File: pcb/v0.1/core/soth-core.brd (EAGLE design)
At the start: 54 x 22 mm, 31 parts, among them IC1 ATXMEGA32E5-AU, M1 SMALL_SERVO, M2 SMALL_SERVO, M3 SMALL_SERVO, M4 SMALL_SERVO, M5 SMALL_SERVO, U1 LDO-TPS78233

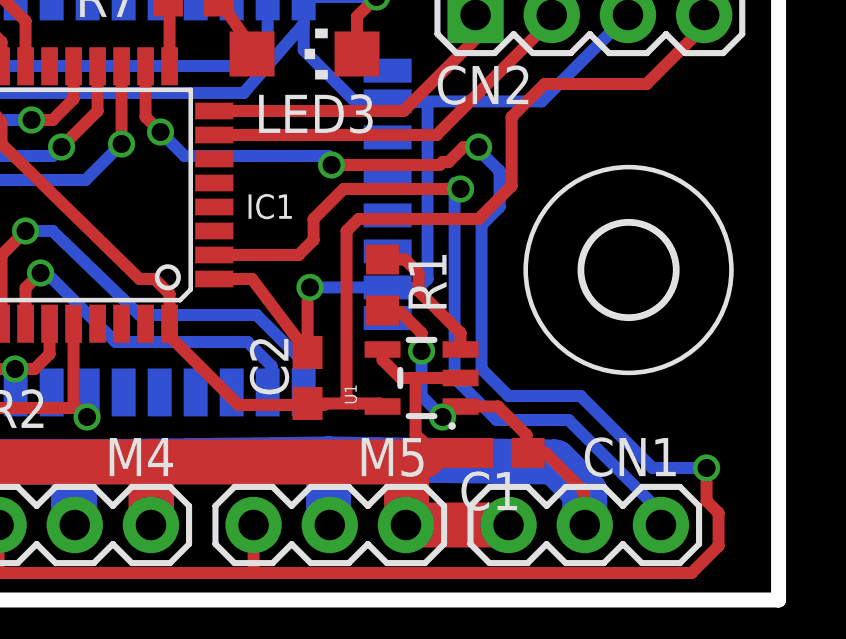
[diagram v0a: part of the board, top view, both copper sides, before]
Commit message: Bugfix pcb design. Replace LDO parts.
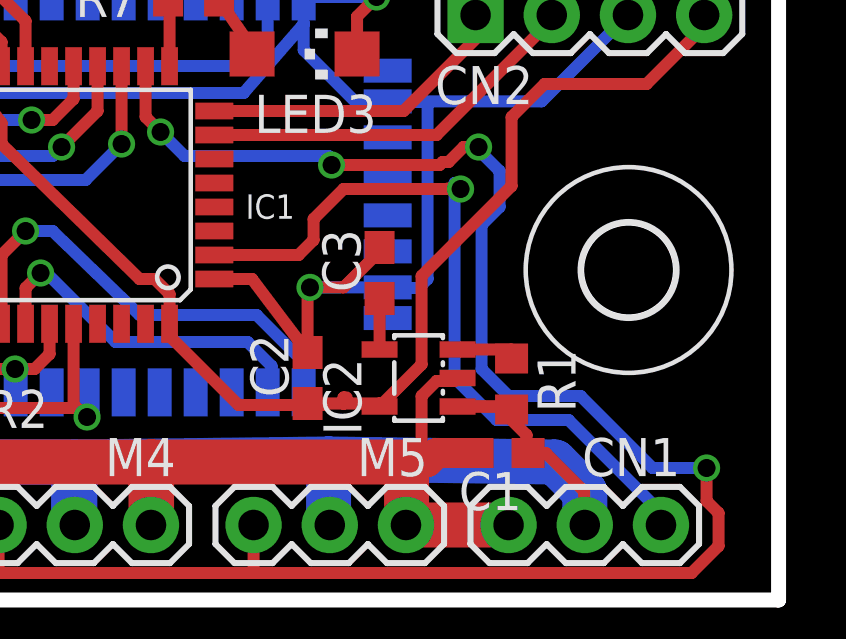
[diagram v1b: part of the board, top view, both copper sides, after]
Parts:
- removed U1: LDO-TPS78233, SparkFun-PowerIC:SOT23-5
- added C3: 0u01, rcl:C1608
- added IC2: TPS77001, texas:SOT23-DBV
- moved R1 5.42 mm to (45.1, 7.20)
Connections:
- new net N$25: C3.1, IC2.4
- net +3V3: now also IC2.5; no longer U1.5
- net +5V: now also IC2.1; no longer U1.1
- net GND: now also IC2.2; no longer U1.2, U1.4
- net GNDA: now also C3.2
- net N$2: now also IC2.3; no longer U1.3
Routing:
- net +5V: track 90.0 -> 86.2 mm, vias 4 -> 2
- net GND: track 83.9 -> 80.3 mm
- net GNDA: track 113.2 -> 116.2 mm
- net +3V3: track 86.2 -> 83.6 mm
- net N$2: track 4.52 -> 2.10 mm
- net N$25: track 0.00 -> 1.70 mm
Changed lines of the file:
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@@
 <attribute name="VALUE" x="43.73" y="-0.675" size="1.27" layer="27"/>
 </element>
-<element name="U1" library="SparkFun-PowerIC" package="SOT23-5" value="LDO-TPS78233" x="42.1" y="7.4" rot="R90"/>
 <element name="C1" library="rcl" package="C1608" value="0u1" x="44.8" y="4.9" rot="R180"/>
 <element name="C2" library="rcl" package="C1608" value="1u" x="38.3" y="7.4" rot="R90"/>
-<element name="R1" library="rcl" package="R0603" value="10k" x="40.8" y="10.5" smashed="yes" rot="R90">
-<attribute name="NAME" x="42.9336" y="9.5602" size="1.27" layer="25" rot="R90"/>
-<attribute name="VALUE" x="42.705" y="9.865" size="1.27" layer="27" rot="R90"/>
+<element name="R1" library="rcl" package="R0603" value="10k" x="45.1" y="7.2" smashed="yes" rot="R90">
+<attribute name="NAME" x="47.2336" y="6.2602" size="1.27" layer="25" rot="R90"/>
+<attribute name="VALUE" x="47.005" y="6.565" size="1.27" layer="27" rot="R90"/>
 </element>
 <element name="CN2" library="SparkFun-Connectors" package="1X04" value="" x="43.9" y="19.5" smashed="yes">
@@
 </element>
 <element name="U$2" library="Soth" package="SILK_LOGO" value="SOTH_LOGO" x="15.0622" y="17.9324"/>
+<element name="IC2" library="texas" package="SOT23-DBV" value="TPS77001" x="42" y="7.4" rot="R90">
+<attribute name="OC_NEWARK" value="77C1171" x="42" y="7.4" size="1.778" layer="27" rot="R90" display="off"/>
+<attribute name="MPN" value="TPS77001DBVT" x="42" y="7.4" size="1.778" layer="27" rot="R90" display="off"/>
+<attribute name="MF" value="TEXAS INSTRUMENTS" x="42" y="7.4" size="1.778" layer="27" rot="R90" display="off"/>
+<attribute name="OC_FARNELL" value="8461554" x="42" y="7.4" size="1.778" layer="27" rot="R90" display="off"/>
+</element>
+<element name="C3" library="rcl" package="C1608" value="0u01" x="40.7" y="10.9" rot="R90"/>
 </elements>
 <signals>
@@
 <wire x1="45" y1="2.5" x2="41.58" y2="2.5" width="1.5" layer="1"/>
 <contactref element="C1" pad="2"/>
-<contactref element="U1" pad="4"/>
-<contactref element="U1" pad="2"/>
 <wire x1="41.6" y1="4.6" x2="42.3" y2="4.6" width="1" layer="1"/>
 <wire x1="42.3" y1="4.6" x2="42.6" y2="4.9" width="1" layer="1"/>
 <wire x1="42.6" y1="4.9" x2="43.95" y2="4.9" width="1" layer="1"/>
-<wire x1="40.7999" y1="8.35" x2="40.7999" y2="8.0001" width="0.4" layer="1"/>
-<wire x1="40.7999" y1="8.0001" x2="41.4" y2="7.4" width="0.4" layer="1"/>
-<wire x1="41.4" y1="7.4" x2="43.4001" y2="7.4" width="0.4" layer="1"/>
-<wire x1="43.4001" y1="7.4" x2="42.1" y2="7.4" width="0.4" layer="1"/>
-<wire x1="42.1" y1="7.4" x2="41.9" y2="7.3" width="0.4" layer="1"/>
-<wire x1="41.9" y1="7.3" x2="41.9" y2="5.5" width="0.4" layer="1"/>
-<wire x1="41.9" y1="5.5" x2="42.6" y2="4.9" width="0.4" layer="1"/>
 <contactref element="T3" pad="2"/>
 <contactref element="T2" pad="2"/>
@@
 <wire x1="4.7" y1="4.892" x2="7.308" y2="4.892" width="0.4" layer="1"/>
 <wire x1="7.308" y1="4.892" x2="7.6" y2="4.6" width="0.4" layer="1"/>
+<contactref element="IC2" pad="2"/>
+<wire x1="42.6" y1="4.9" x2="42.1" y2="4.9" width="0.4" layer="1"/>
+<wire x1="42.1" y1="4.9" x2="42.1" y2="6.8" width="0.4" layer="1"/>
+<wire x1="42.1" y1="6.8" x2="42.6" y2="7.3" width="0.4" layer="1"/>
+<wire x1="42.6" y1="7.3" x2="43.2" y2="7.3" width="0.4" layer="1"/>
+<wire x1="43.2" y1="7.3" x2="43.3" y2="7.4" width="0.4" layer="1"/>
 </signal>
 <signal name="GNDA" class="4">
@@
 <vertex x="0" y="0"/>
 </polygon>
+<contactref element="C3" pad="2"/>
+<wire x1="40.7" y1="11.75" x2="40.7" y2="11.62" width="0.4" layer="1"/>
+<wire x1="40.7" y1="11.62" x2="39.5" y2="10.42" width="0.4" layer="1"/>
+<wire x1="39.5" y1="10.42" x2="38.38" y2="10.42" width="0.4" layer="1"/>
 </signal>
 <signal name="+3V3" class="3">
 <contactref element="IC1" pad="17"/>
 <contactref element="IC1" pad="32"/>
-<contactref element="U1" pad="5"/>
 <contactref element="C2" pad="1"/>
-<wire x1="38.3" y1="6.55" x2="39.9" y2="6.55" width="0.4" layer="1"/>
-<wire x1="39.9" y1="6.55" x2="40.6999" y2="6.55" width="0.4" layer="1"/>
-<wire x1="40.6999" y1="6.55" x2="40.7999" y2="6.45" width="0.4" layer="1"/>
 <contactref element="U$1" pad="11"/>
 <contactref element="CN2" pad="4"/>
@@
 <wire x1="51.52" y1="19.12" x2="49.6" y2="17.2" width="0.4" layer="1"/>
 <wire x1="49.6" y1="17.2" x2="46.2" y2="17.2" width="0.4" layer="1"/>
-<wire x1="39.6" y1="6.75" x2="39.9" y2="6.55" width="0.4" layer="1"/>
 <contactref element="R6" pad="2"/>
 <contactref element="R5" pad="2"/>
-<wire x1="39.6" y1="6.75" x2="39.6" y2="12.3" width="0.4" layer="1"/>
-<wire x1="39.6" y1="12.3" x2="40" y2="12.7" width="0.4" layer="1"/>
-<wire x1="40" y1="12.7" x2="44" y2="12.7" width="0.4" layer="1"/>
-<wire x1="44" y1="12.7" x2="45.1" y2="13.8" width="0.4" layer="1"/>
 <wire x1="45.1" y1="13.8" x2="45.1" y2="16.1" width="0.4" layer="1"/>
 <wire x1="45.1" y1="16.1" x2="46.2" y2="17.2" width="0.4" layer="1"/>
@@
 <wire x1="23.9" y1="18.3" x2="26.3" y2="18.3" width="0.4" layer="1"/>
 <wire x1="26.3" y1="18.3" x2="26.6" y2="18" width="0.4" layer="1"/>
+<contactref element="IC2" pad="5"/>
+<wire x1="38.3" y1="6.55" x2="39.5" y2="6.55" width="0.4064" layer="1"/>
+<wire x1="39.5" y1="6.55" x2="40.7" y2="6.55" width="0.4064" layer="1"/>
+<wire x1="40.7" y1="6.55" x2="40.7" y2="6.45" width="0.4064" layer="1"/>
+<wire x1="39.6" y1="6.75" x2="39.5" y2="6.75" width="0.4064" layer="1"/>
+<wire x1="39.5" y1="6.75" x2="39.5" y2="6.55" width="0.4064" layer="1"/>
+<wire x1="45.1" y1="13.8" x2="42.1" y2="10.8" width="0.4" layer="1"/>
+<wire x1="42.1" y1="10.8" x2="42.1" y2="7.85" width="0.4" layer="1"/>
+<wire x1="42.1" y1="7.85" x2="40.7" y2="6.45" width="0.4" layer="1"/>
 </signal>
 <signal name="+5V" class="1">
@@
 <wire x1="46.54" y1="4.6" x2="47.54" y2="3.6" width="1.5" layer="16"/>
 <wire x1="47.54" y1="3.6" x2="47.54" y2="2.5" width="1.5" layer="16"/>
-<contactref element="U1" pad="1"/>
 <contactref element="C1" pad="1"/>
-<contactref element="R1" pad="1"/>
 <wire x1="45.65" y1="4.9" x2="46.24" y2="4.9" width="0.4" layer="1"/>
 <wire x1="46.24" y1="4.9" x2="47.52" y2="3.62" width="0.4" layer="1"/>
 <wire x1="47.52" y1="3.62" x2="47.52" y2="2.52" width="0.4" layer="1"/>
 <wire x1="47.52" y1="2.52" x2="47.54" y2="2.5" width="0.4" layer="1"/>
-<wire x1="40.8" y1="9.65" x2="41.15" y2="9.65" width="0.4" layer="1"/>
-<wire x1="43.3501" y1="6.5" x2="43.4001" y2="6.45" width="0.4" layer="1"/>
-<wire x1="43.4001" y1="6.45" x2="44.65" y2="6.45" width="0.4" layer="1"/>
 <wire x1="44.65" y1="6.45" x2="45.6" y2="5.5" width="0.4" layer="1"/>
 <wire x1="45.6" y1="5.5" x2="45.6" y2="4.95" width="0.4" layer="1"/>
 <wire x1="45.6" y1="4.95" x2="45.65" y2="4.9" width="0.4" layer="1"/>
-<wire x1="43.3501" y1="6.5" x2="43.2" y2="6.5" width="0.4" layer="1"/>
-<wire x1="43.2" y1="6.5" x2="42.8" y2="6.1" width="0.4" layer="1"/>
-<via x="42.8" y="6.1" extent="1-16" drill="0.6"/>
-<wire x1="42.8" y1="6.1" x2="42.1" y2="6.8" width="0.4" layer="16"/>
-<wire x1="42.1" y1="6.8" x2="42.1" y2="8.3" width="0.4" layer="16"/>
-<via x="42.1" y="8.3" extent="1-16" drill="0.6"/>
-<wire x1="42.1" y1="8.3" x2="42.1" y2="8.9" width="0.4" layer="1"/>
-<wire x1="42.1" y1="8.9" x2="41.4" y2="9.6" width="0.4" layer="1"/>
-<wire x1="41.4" y1="9.6" x2="40.85" y2="9.6" width="0.4" layer="1"/>
-<wire x1="40.85" y1="9.6" x2="40.8" y2="9.65" width="0.4" layer="1"/>
 <contactref element="CN4" pad="1"/>
 <wire x1="5.04" y1="4.6" x2="4.14" y2="5.16" width="1" layer="16"/>
@@
 <wire x1="4.14" y1="5.16" x2="4.14" y2="8.74" width="1" layer="16"/>
 <wire x1="4.14" y1="8.74" x2="4.5" y2="9.1" width="1" layer="16"/>
-</signal>
-<signal name="N$2">
-<contactref element="R1" pad="2"/>
-<contactref element="U1" pad="3"/>
-<wire x1="40.8" y1="11.35" x2="41.55" y2="11.35" width="0.4" layer="1"/>
-<wire x1="41.55" y1="11.35" x2="42" y2="10.9" width="0.4" layer="1"/>
-<wire x1="42" y1="10.9" x2="42" y2="10.3" width="0.4" layer="1"/>
-<wire x1="42" y1="10.3" x2="43.4" y2="8.9" width="0.4" layer="1"/>
-<wire x1="43.4" y1="8.9" x2="43.4" y2="8.3501" width="0.4" layer="1"/>
-<wire x1="43.4" y1="8.3501" x2="43.4001" y2="8.35" width="0.4" layer="1"/>
+<contactref element="R1" pad="1"/>
+<contactref element="IC2" pad="1"/>
+<wire x1="43.3" y1="6.45" x2="44.65" y2="6.45" width="0.4064" layer="1"/>
+<wire x1="43.3" y1="6.45" x2="45.1" y2="6.45" width="0.4" layer="1"/>
+<wire x1="45.1" y1="6.45" x2="45.1" y2="6.35" width="0.4" layer="1"/>
 </signal>
 <signal name="N$4">
@@
 <wire x1="36.45" y1="18.4" x2="36.45" y2="18.2" width="0.4" layer="1"/>
 </signal>
+<signal name="N$2">
+<contactref element="R1" pad="2"/>
+<contactref element="IC2" pad="3"/>
+<wire x1="43.3" y1="8.35" x2="45.1" y2="8.35" width="0.4" layer="1"/>
+<wire x1="45.1" y1="8.35" x2="45.1" y2="8.05" width="0.4" layer="1"/>
+</signal>
+<signal name="N$25">
+<contactref element="IC2" pad="4"/>
+<contactref element="C3" pad="1"/>
+<wire x1="40.7" y1="10.05" x2="40.7" y2="8.35" width="0.4" layer="1"/>
+</signal>
 </signals>

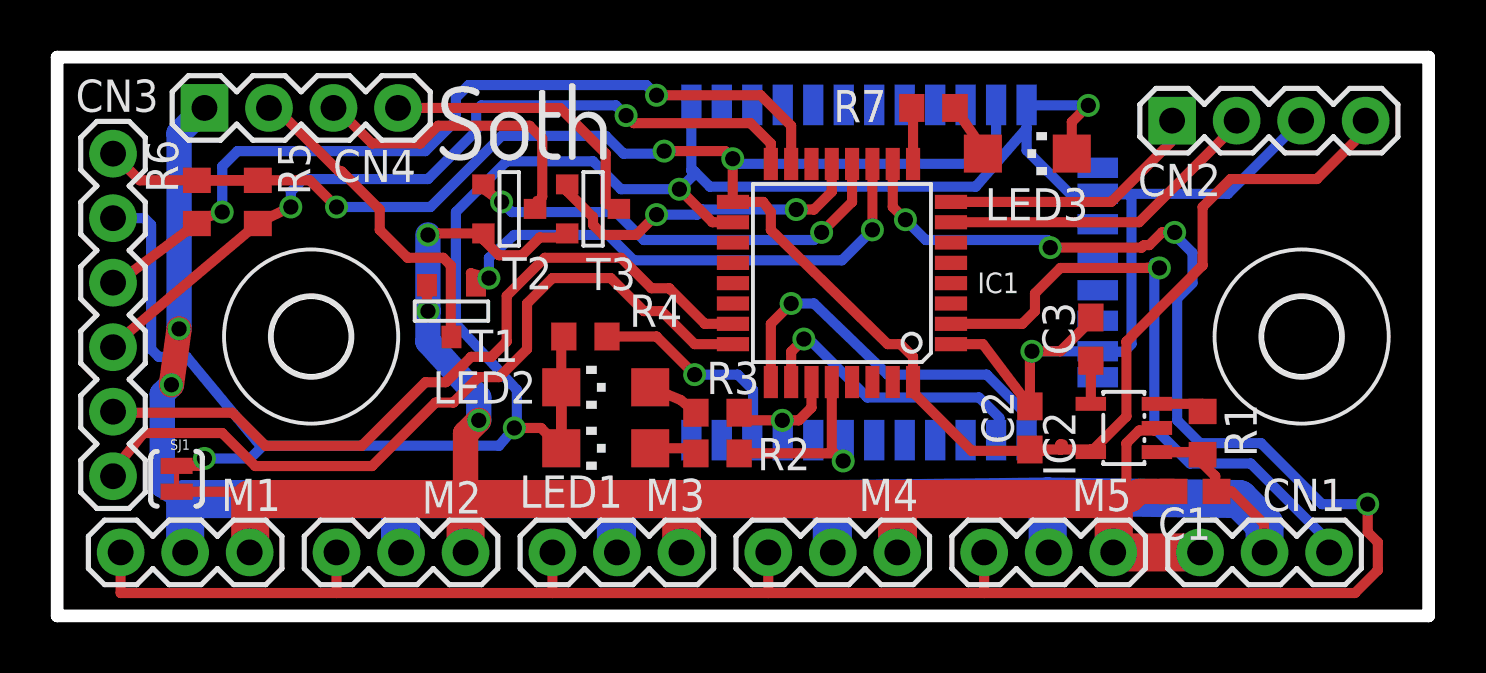
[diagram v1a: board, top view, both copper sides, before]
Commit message: Change microcontroller from atxmega32d4 to atxmega32e5
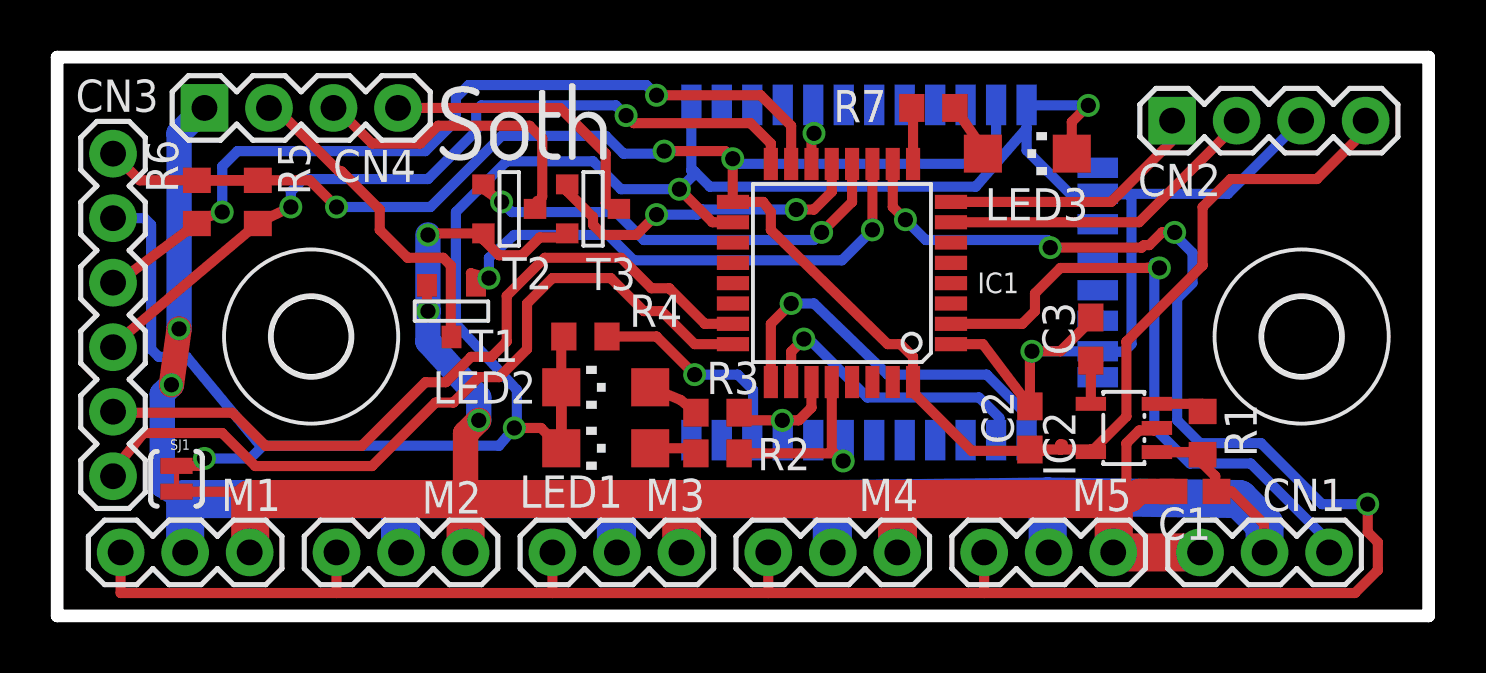
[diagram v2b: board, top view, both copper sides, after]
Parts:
- LED1: value RED CONNECT -> GREEN CONNECTED
- LED2: value GREEN CONNECTED -> RED CONNECT
- LED3: value GREEN STATUS -> YELLOW STATUS
- R2, R3, R7: value 1k -> 2k
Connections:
- new net N$26: IC1.14, U$1.5
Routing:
- net N$26: track 0.00 -> 2.38 mm, vias 0 -> 1
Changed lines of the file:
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@@
 <attribute name="VALUE" x="42.63" y="16.325" size="1.27" layer="27"/>
 </element>
-<element name="R2" library="rcl" package="R0603" value="1k" x="26" y="6.4" smashed="yes">
+<element name="R2" library="rcl" package="R0603" value="2k" x="26" y="6.4" smashed="yes">
 <attribute name="NAME" x="27.565" y="5.735" size="1.27" layer="25"/>
 <attribute name="VALUE" x="25.365" y="4.495" size="1.27" layer="27"/>
 </element>
-<element name="R3" library="rcl" package="R0603" value="1k" x="26" y="8" smashed="yes">
+<element name="R3" library="rcl" package="R0603" value="2k" x="26" y="8" smashed="yes">
 <attribute name="NAME" x="25.565" y="8.735" size="1.27" layer="25"/>
 <attribute name="VALUE" x="25.365" y="6.095" size="1.27" layer="27"/>
 </element>
-<element name="LED1" library="led" package="CHIPLED_1206" value="RED CONNECT" x="21.6" y="6.6" smashed="yes" rot="R90">
+<element name="LED1" library="led" package="CHIPLED_1206" value="GREEN CONNECTED" x="21.6" y="6.6" smashed="yes" rot="R90">
 <attribute name="NAME" x="22.27" y="5.53" size="1.27" layer="25" rot="R180"/>
 <attribute name="VALUE" x="22.87" y="9.14" size="1.27" layer="27" rot="R180"/>
 </element>
-<element name="LED2" library="led" package="CHIPLED_1206" value="GREEN CONNECTED" x="21.6" y="9" smashed="yes" rot="R90">
+<element name="LED2" library="led" package="CHIPLED_1206" value="RED CONNECT" x="21.6" y="9" smashed="yes" rot="R90">
 <attribute name="NAME" x="18.854" y="9.63" size="1.27" layer="25" rot="R180"/>
 <attribute name="VALUE" x="22.87" y="11.54" size="1.27" layer="27" rot="R180"/>
@@
 <attribute name="VALUE" x="6.351" y="4.4475" size="0.4064" layer="27" rot="R90"/>
 </element>
-<element name="LED3" library="led" package="CHIPLED_1206" value="GREEN STATUS" x="38.2" y="18.2" smashed="yes" rot="R270">
+<element name="LED3" library="led" package="CHIPLED_1206" value="YELLOW STATUS" x="38.2" y="18.2" smashed="yes" rot="R270">
 <attribute name="NAME" x="36.53" y="15.57" size="1.27" layer="25"/>
 <attribute name="VALUE" x="36.93" y="15.66" size="1.27" layer="27"/>
 </element>
-<element name="R7" library="rcl" package="R0603" value="1k" x="34.5" y="20" smashed="yes">
+<element name="R7" library="rcl" package="R0603" value="2k" x="34.5" y="20" smashed="yes">
 <attribute name="NAME" x="30.565" y="19.435" size="1.27" layer="25"/>
 <attribute name="VALUE" x="33.865" y="18.095" size="1.27" layer="27"/>
@@
 </signal>
 <signal name="N$7">
-<contactref element="U$1" pad="21"/>
 <contactref element="R3" pad="2"/>
 <contactref element="IC1" pad="27"/>
 <via x="28.55" y="7.7" extent="1-16" drill="0.6"/>
 <wire x1="28.55" y1="7.7" x2="28.5" y2="6.99" width="0.4" layer="16"/>
-<wire x1="28.5" y1="6.99" x2="28.57" y2="6.92" width="0.4" layer="16"/>
 <wire x1="29.7" y1="9.2074" x2="29.7" y2="8.2" width="0.4" layer="1"/>
 <wire x1="29.7" y1="8.2" x2="29.2" y2="7.7" width="0.4" layer="1"/>
@@
 <wire x1="28.55" y1="7.7" x2="27.05" y2="7.7" width="0.4" layer="1"/>
 <wire x1="27.05" y1="7.7" x2="26.85" y2="8" width="0.4" layer="1"/>
+<contactref element="U$1" pad="21"/>
+<wire x1="28.57" y1="6.92" x2="28.5" y2="6.99" width="0" layer="19" extent="16-16"/>
 </signal>
 <signal name="N$8">
@@
 <wire x1="40.7" y1="10.05" x2="40.7" y2="8.35" width="0.4" layer="1"/>
 </signal>
+<signal name="N$26">
+<contactref element="IC1" pad="14"/>
+<contactref element="U$1" pad="5"/>
+<wire x1="29.7" y1="17.7926" x2="29.7" y2="18.9" width="0.4" layer="1"/>
+<wire x1="29.7" y1="18.9" x2="29.8" y2="19" width="0.4" layer="1"/>
+<via x="29.8" y="19" extent="1-16" drill="0.6"/>
+<wire x1="29.8" y1="19" x2="29.8" y2="20.09" width="0.4" layer="16"/>
+<wire x1="29.8" y1="20.09" x2="29.77" y2="20.12" width="0.4" layer="16"/>
+</signal>
 </signals>
